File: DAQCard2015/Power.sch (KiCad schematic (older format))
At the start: 33 parts, among them CON1 BARREL_JACK, SW1 SPST, U18 APXS002A0X-SRZ, U19 APXS002A0X-SRZ, U20 APXS002A0X-SRZ, U21 CDBHD240-G, U23 LM1086

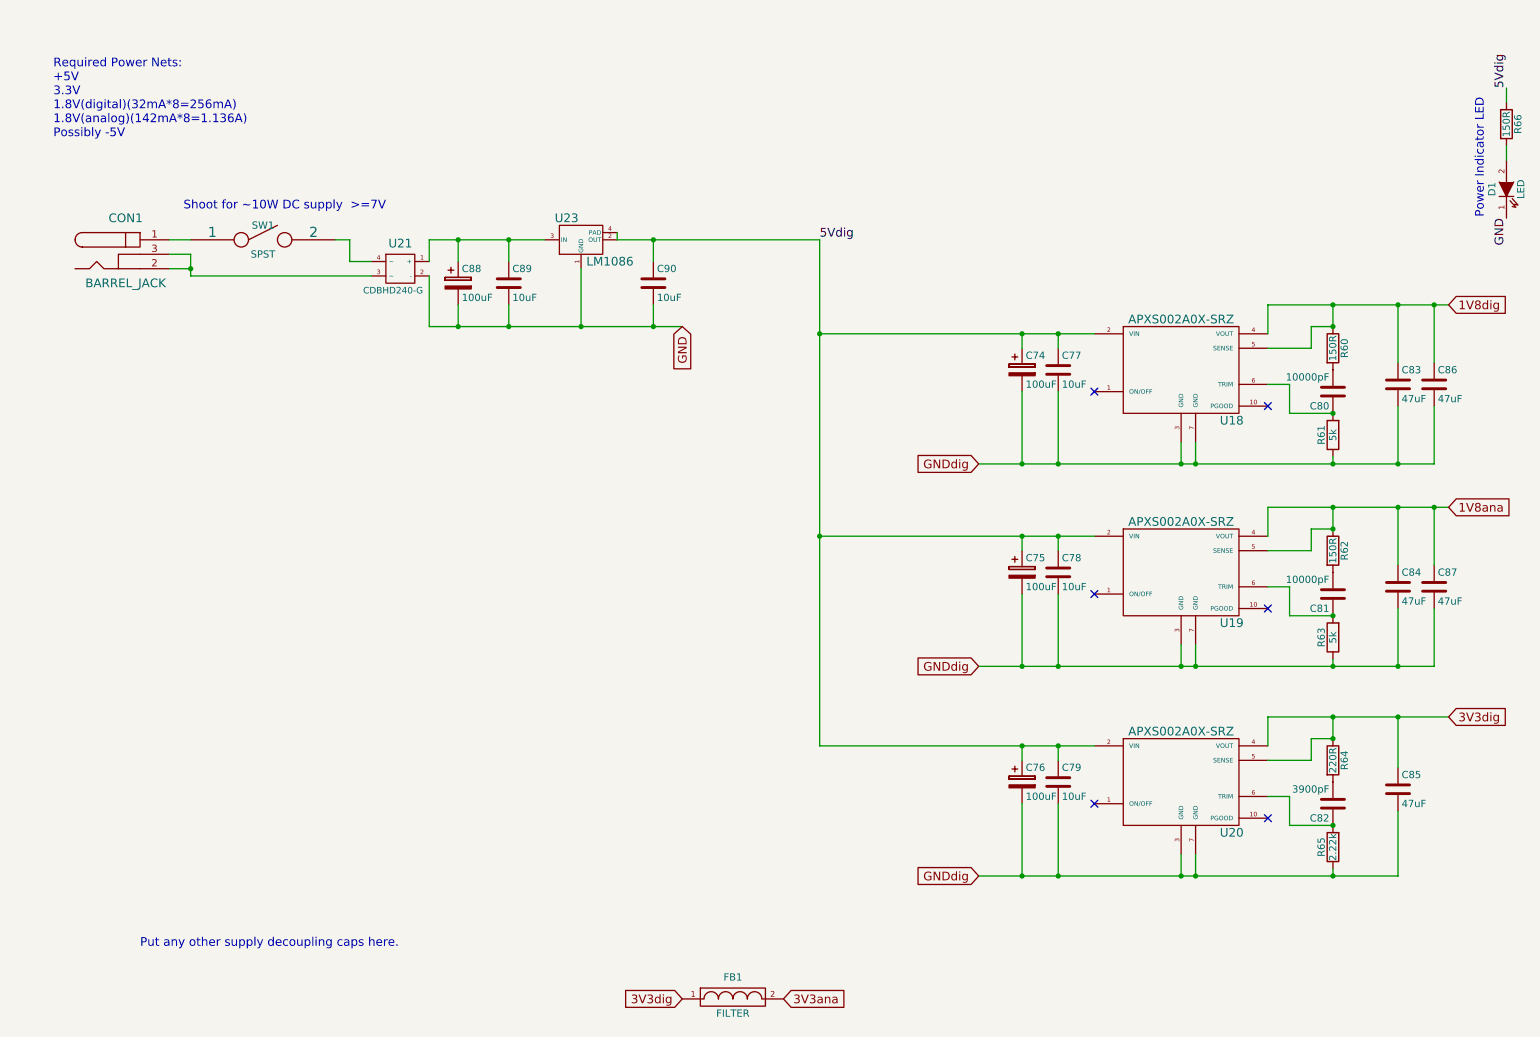
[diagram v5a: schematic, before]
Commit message: propogate previous changes to other channels and schematic
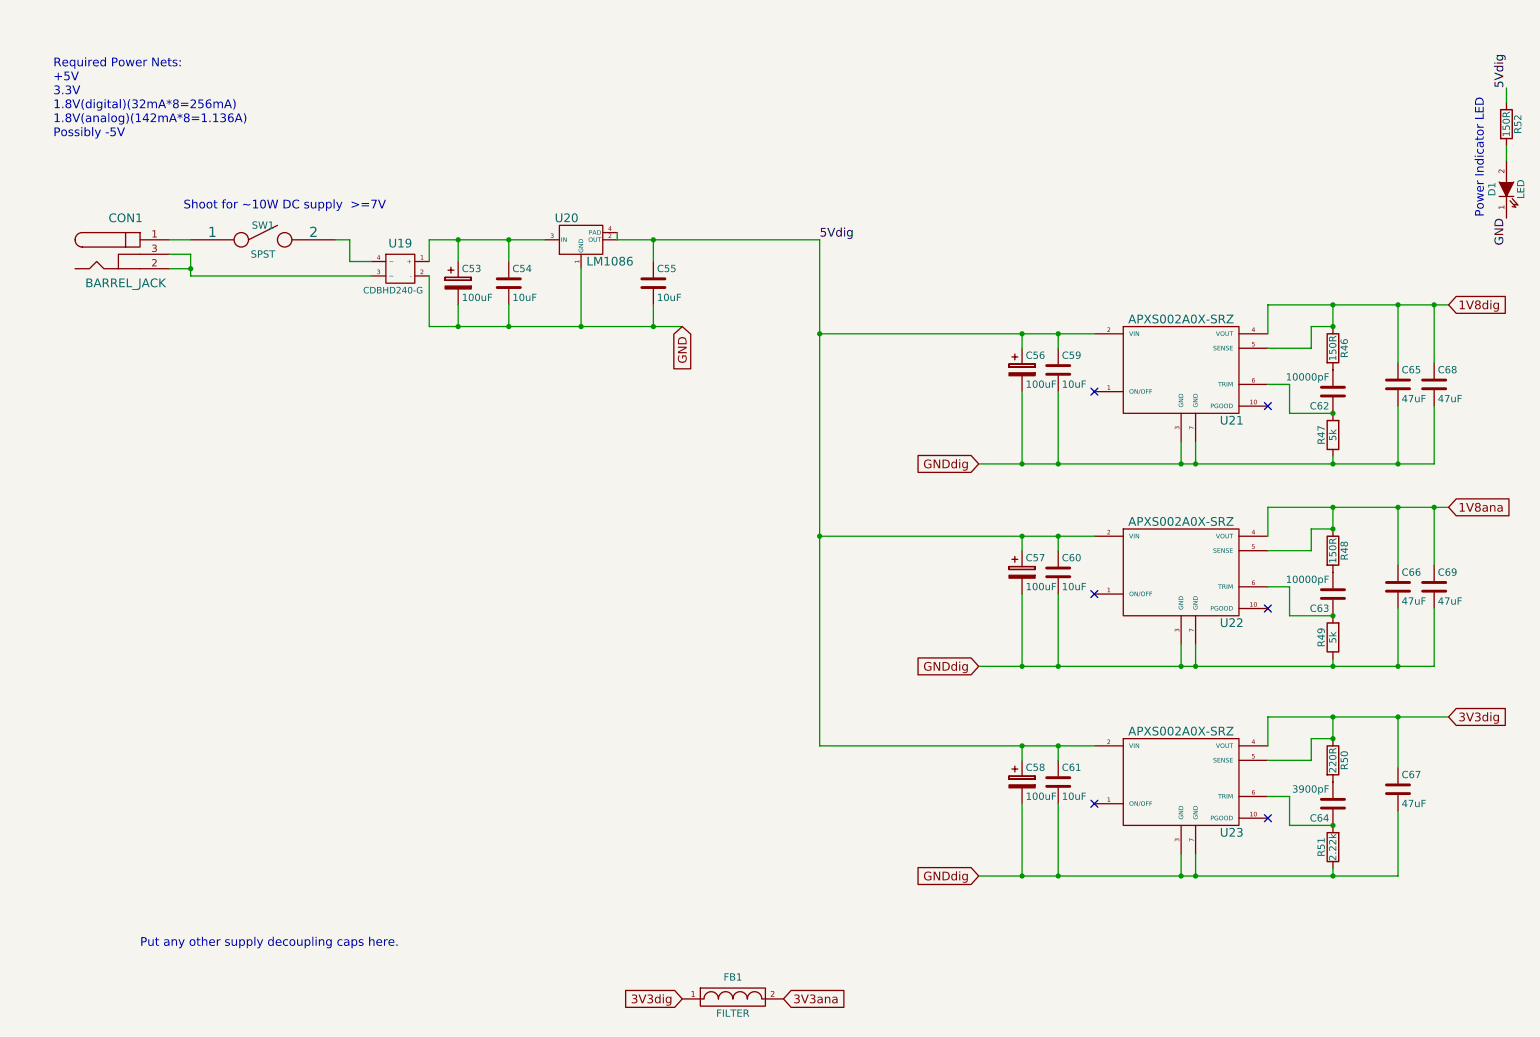
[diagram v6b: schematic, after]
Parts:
- C54: renamed from C89; footprint (none) -> Capacitors_SMD:C_0805
- C55: renamed from C90; footprint (none) -> Capacitors_SMD:C_0805
- renumbered C88 to C53, C74 to C56, C75 to C57, C76 to C58, C77 to C59, C78 to C60, C79 to C61, C80 to C62, C81 to C63, C82 to C64, C83 to C65, C84 to C66, C85 to C67, C86 to C68, C87 to C69, R60 to R46, R61 to R47, R62 to R48, R63 to R49, R64 to R50, R65 to R51, R66 to R52, U21 to U19, U23 to U20, U18 to U21, U19 to U22, U20 to U23
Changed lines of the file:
@@
 Required Power Nets:\n+5V\n3.3V\n1.8V(digital)(32mA*8=256mA)\n1.8V(analog)(142mA*8=1.136A)\nPossibly -5V
 $Comp
-L APXS002A0X-SRZ U18
+L APXS002A0X-SRZ U21
 U 1 1 55CC1B62
 P 8750 2750
-F 0 "U18" H 9100 2400 60  0000 C CNN
+F 0 "U21" H 9100 2400 60  0000 C CNN
 F 1 "APXS002A0X-SRZ" H 8750 3100 60  0000 C CNN
 F 2 "extras:APXS002A0X-SRZ" H 8400 2100 60  0001 C CNN
@@
 $EndComp
 $Comp
-L CP C74
+L CP C56
 U 1 1 55CC28F2
 P 7650 2750
-F 0 "C74" H 7675 2850 50  0000 L CNN
+F 0 "C56" H 7675 2850 50  0000 L CNN
 F 1 "100uF" H 7675 2650 50  0000 L CNN
 F 2 "extras:SMD_Cap_8mmDia" H 7688 2600 30  0001 C CNN
@@
 $EndComp
 $Comp
-L C C77
+L C C59
 U 1 1 55CC2951
 P 7900 2750
-F 0 "C77" H 7925 2850 50  0000 L CNN
+F 0 "C59" H 7925 2850 50  0000 L CNN
 F 1 "10uF" H 7925 2650 50  0000 L CNN
 F 2 "Capacitors_SMD:C_0805" H 7938 2600 30  0001 C CNN
@@
 $EndComp
 $Comp
-L R R60
+L R R46
 U 1 1 55CC29C3
 P 9800 2600
-F 0 "R60" V 9880 2600 50  0000 C CNN
+F 0 "R46" V 9880 2600 50  0000 C CNN
 F 1 "150R" V 9800 2600 50  0000 C CNN
 F 2 "Resistors_SMD:R_0603" V 9730 2600 30  0001 C CNN
@@
 $EndComp
 $Comp
-L R R61
+L R R47
 U 1 1 55CC2A10
 P 9800 3200
-F 0 "R61" V 9880 3200 50  0000 C CNN
+F 0 "R47" V 9880 3200 50  0000 C CNN
 F 1 "5k" V 9800 3200 50  0000 C CNN
 F 2 "Resistors_SMD:R_0603" V 9730 3200 30  0001 C CNN
@@
 $EndComp
 $Comp
-L C C80
+L C C62
 U 1 1 55CC2A89
 P 9800 2900
-F 0 "C80" H 9825 3000 50  0000 L CNN
+F 0 "C62" H 9825 3000 50  0000 L CNN
 F 1 "10000pF" H 9825 2800 50  0000 L CNN
 F 2 "Capacitors_SMD:C_0603" H 9838 2750 30  0001 C CNN
@@
 $EndComp
 $Comp
-L C C83
+L C C65
 U 1 1 55CC2AEA
 P 10250 2850
-F 0 "C83" H 10275 2950 50  0000 L CNN
+F 0 "C65" H 10275 2950 50  0000 L CNN
 F 1 "47uF" H 10275 2750 50  0000 L CNN
 F 2 "extras:SMD_Cap_8mmDia" H 10288 2700 30  0001 C CNN
@@
 Connection ~ 7650 3400
 $Comp
-L C C86
+L C C68
 U 1 1 55CC4361
 P 10500 2850
-F 0 "C86" H 10525 2950 50  0000 L CNN
+F 0 "C68" H 10525 2950 50  0000 L CNN
 F 1 "47uF" H 10525 2750 50  0000 L CNN
 F 2 "extras:SMD_Cap_8mmDia" H 10538 2700 30  0001 C CNN
@@
 GNDdig
 $Comp
-L APXS002A0X-SRZ U19
+L APXS002A0X-SRZ U22
 U 1 1 55CC74F0
 P 8750 4150
-F 0 "U19" H 9100 3800 60  0000 C CNN
+F 0 "U22" H 9100 3800 60  0000 C CNN
 F 1 "APXS002A0X-SRZ" H 8750 4500 60  0000 C CNN
 F 2 "extras:APXS002A0X-SRZ" H 8400 3500 60  0001 C CNN
@@
 $EndComp
 $Comp
-L CP C75
+L CP C57
 U 1 1 55CC74F7
 P 7650 4150
-F 0 "C75" H 7675 4250 50  0000 L CNN
+F 0 "C57" H 7675 4250 50  0000 L CNN
 F 1 "100uF" H 7675 4050 50  0000 L CNN
 F 2 "extras:SMD_Cap_8mmDia" H 7688 4000 30  0001 C CNN
@@
 $EndComp
 $Comp
-L C C78
+L C C60
 U 1 1 55CC74FD
 P 7900 4150
-F 0 "C78" H 7925 4250 50  0000 L CNN
+F 0 "C60" H 7925 4250 50  0000 L CNN
 F 1 "10uF" H 7925 4050 50  0000 L CNN
 F 2 "Capacitors_SMD:C_0805" H 7938 4000 30  0001 C CNN
@@
 $EndComp
 $Comp
-L R R62
+L R R48
 U 1 1 55CC7503
 P 9800 4000
-F 0 "R62" V 9880 4000 50  0000 C CNN
+F 0 "R48" V 9880 4000 50  0000 C CNN
 F 1 "150R" V 9800 4000 50  0000 C CNN
 F 2 "Resistors_SMD:R_0603" V 9730 4000 30  0001 C CNN
@@
 $EndComp
 $Comp
-L R R63
+L R R49
 U 1 1 55CC7509
 P 9800 4600
-F 0 "R63" V 9880 4600 50  0000 C CNN
+F 0 "R49" V 9880 4600 50  0000 C CNN
 F 1 "5k" V 9800 4600 50  0000 C CNN
 F 2 "Resistors_SMD:R_0603" V 9730 4600 30  0001 C CNN
@@
 $EndComp
 $Comp
-L C C81
+L C C63
 U 1 1 55CC750F
 P 9800 4300
-F 0 "C81" H 9825 4400 50  0000 L CNN
+F 0 "C63" H 9825 4400 50  0000 L CNN
 F 1 "10000pF" H 9825 4200 50  0000 L CNN
 F 2 "Capacitors_SMD:C_0603" H 9838 4150 30  0001 C CNN
@@
 $EndComp
 $Comp
-L C C84
+L C C66
 U 1 1 55CC7515
 P 10250 4250
-F 0 "C84" H 10275 4350 50  0000 L CNN
+F 0 "C66" H 10275 4350 50  0000 L CNN
 F 1 "47uF" H 10275 4150 50  0000 L CNN
 F 2 "extras:SMD_Cap_8mmDia" H 10288 4100 30  0001 C CNN
@@
 Connection ~ 7650 4800
 $Comp
-L C C87
+L C C69
 U 1 1 55CC7546
 P 10500 4250
-F 0 "C87" H 10525 4350 50  0000 L CNN
+F 0 "C69" H 10525 4350 50  0000 L CNN
 F 1 "47uF" H 10525 4150 50  0000 L CNN
 F 2 "extras:SMD_Cap_8mmDia" H 10538 4100 30  0001 C CNN
@@
 GNDdig
 $Comp
-L APXS002A0X-SRZ U20
+L APXS002A0X-SRZ U23
 U 1 1 55CC7C26
 P 8750 5600
-F 0 "U20" H 9100 5250 60  0000 C CNN
+F 0 "U23" H 9100 5250 60  0000 C CNN
 F 1 "APXS002A0X-SRZ" H 8750 5950 60  0000 C CNN
 F 2 "extras:APXS002A0X-SRZ" H 8400 4950 60  0001 C CNN
@@
 $EndComp
 $Comp
-L CP C76
+L CP C58
 U 1 1 55CC7C2D
 P 7650 5600
-F 0 "C76" H 7675 5700 50  0000 L CNN
+F 0 "C58" H 7675 5700 50  0000 L CNN
 F 1 "100uF" H 7675 5500 50  0000 L CNN
 F 2 "extras:SMD_Cap_8mmDia" H 7688 5450 30  0001 C CNN
@@
 $EndComp
 $Comp
-L C C79
+L C C61
 U 1 1 55CC7C33
 P 7900 5600
-F 0 "C79" H 7925 5700 50  0000 L CNN
+F 0 "C61" H 7925 5700 50  0000 L CNN
 F 1 "10uF" H 7925 5500 50  0000 L CNN
 F 2 "Capacitors_SMD:C_0805" H 7938 5450 30  0001 C CNN
@@
 $EndComp
 $Comp
-L R R64
+L R R50
 U 1 1 55CC7C39
 P 9800 5450
-F 0 "R64" V 9880 5450 50  0000 C CNN
+F 0 "R50" V 9880 5450 50  0000 C CNN
 F 1 "220R" V 9800 5450 50  0000 C CNN
 F 2 "Resistors_SMD:R_0603" V 9730 5450 30  0001 C CNN
@@
 $EndComp
 $Comp
-L R R65
+L R R51
 U 1 1 55CC7C3F
 P 9800 6050
-F 0 "R65" V 9880 6050 50  0000 C CNN
+F 0 "R51" V 9880 6050 50  0000 C CNN
 F 1 "2.22k" V 9800 6050 50  0000 C CNN
 F 2 "Resistors_SMD:R_0603" V 9730 6050 30  0001 C CNN
@@
 $EndComp
 $Comp
-L C C82
+L C C64
 U 1 1 55CC7C45
 P 9800 5750
-F 0 "C82" H 9825 5850 50  0000 L CNN
+F 0 "C64" H 9825 5850 50  0000 L CNN
 F 1 "3900pF" H 9825 5650 50  0000 L CNN
 F 2 "Capacitors_SMD:C_0603" H 9838 5600 30  0001 C CNN
@@
 $EndComp
 $Comp
-L C C85
+L C C67
 U 1 1 55CC7C4B
 P 10250 5650
-F 0 "C85" H 10275 5750 50  0000 L CNN
+F 0 "C67" H 10275 5750 50  0000 L CNN
 F 1 "47uF" H 10275 5550 50  0000 L CNN
 F 2 "extras:SMD_Cap_8mmDia" H 10288 5500 30  0001 C CNN
@@
 Shoot for ~~10W DC supply  >=7V
 $Comp
-L CP C88
+L CP C53
 U 1 1 55CD0228
 P 3750 2150
-F 0 "C88" H 3775 2250 50  0000 L CNN
+F 0 "C53" H 3775 2250 50  0000 L CNN
 F 1 "100uF" H 3775 2050 50  0000 L CNN
 F 2 "extras:SMD_Cap_8mmDia" H 3788 2000 30  0001 C CNN
@@
 $EndComp
 $Comp
-L LM1086 U23
+L LM1086 U20
 U 1 1 55EA84EC
 P 4600 2050
-F 0 "U23" H 4500 2400 60  0000 C CNN
+F 0 "U20" H 4500 2400 60  0000 C CNN
 F 1 "LM1086" H 4800 2100 60  0000 C CNN
 F 2 "extras:TO-263-4" H 4600 2050 60  0001 C CNN
@@
 Connection ~ 4100 1850
 $Comp
-L R R66
+L R R52
 U 1 1 55EAAA38
 P 11000 1050
-F 0 "R66" V 11080 1050 50  0000 C CNN
+F 0 "R52" V 11080 1050 50  0000 C CNN
 F 1 "150R" V 11000 1050 50  0000 C CNN
 F 2 "Resistors_SMD:R_0603" V 10930 1050 30  0001 C CNN
@@
 Connection ~ 5100 2450
 $Comp
-L CDBHD240-G U21
+L CDBHD240-G U19
 U 1 1 55EAC9BE
 P 3350 2050
-F 0 "U21" H 3350 2225 60  0000 C CNN
+F 0 "U19" H 3350 2225 60  0000 C CNN
 F 1 "CDBHD240-G" H 3400 1900 45  0000 C CNN
 F 2 "extras:mini-DIP4" H 3350 2050 60  0001 C CNN
@@
 	4850 1850 4850 1800
 $Comp
-L C C89
+L C C54
 U 1 1 55EB2165
 P 4100 2150
-F 0 "C89" H 4125 2250 50  0000 L CNN
+F 0 "C54" H 4125 2250 50  0000 L CNN
 F 1 "10uF" H 4125 2050 50  0000 L CNN
-F 2 "" H 4138 2000 30  0000 C CNN
+F 2 "Capacitors_SMD:C_0805" H 4138 2000 30  0001 C CNN
 F 3 "" H 4100 2150 60  0000 C CNN
 	1    4100 2150
@@
 $EndComp
 $Comp
-L C C90
+L C C55
 U 1 1 55EB21EC
 P 5100 2150
-F 0 "C90" H 5125 2250 50  0000 L CNN
+F 0 "C55" H 5125 2250 50  0000 L CNN
 F 1 "10uF" H 5125 2050 50  0000 L CNN
-F 2 "" H 5138 2000 30  0000 C CNN
+F 2 "Capacitors_SMD:C_0805" H 5138 2000 30  0001 C CNN
 F 3 "" H 5100 2150 60  0000 C CNN
 	1    5100 2150

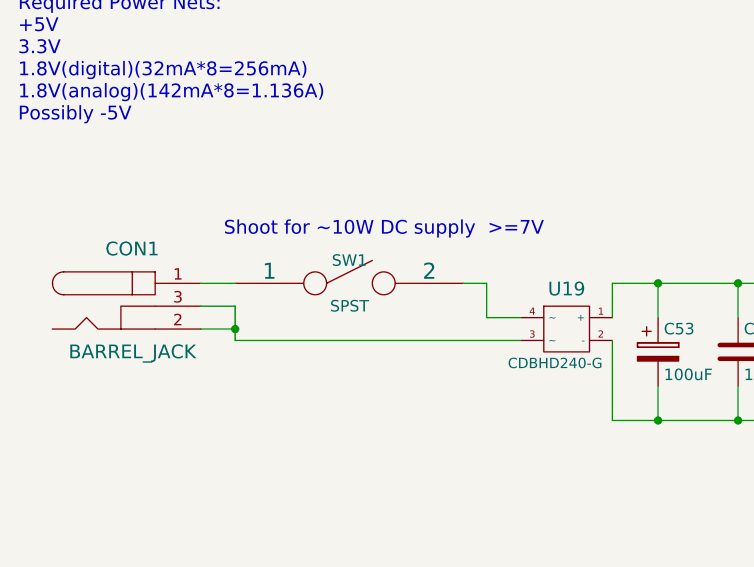
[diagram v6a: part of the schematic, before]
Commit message: Reroutes LVDS signals to give pairs proper impedances
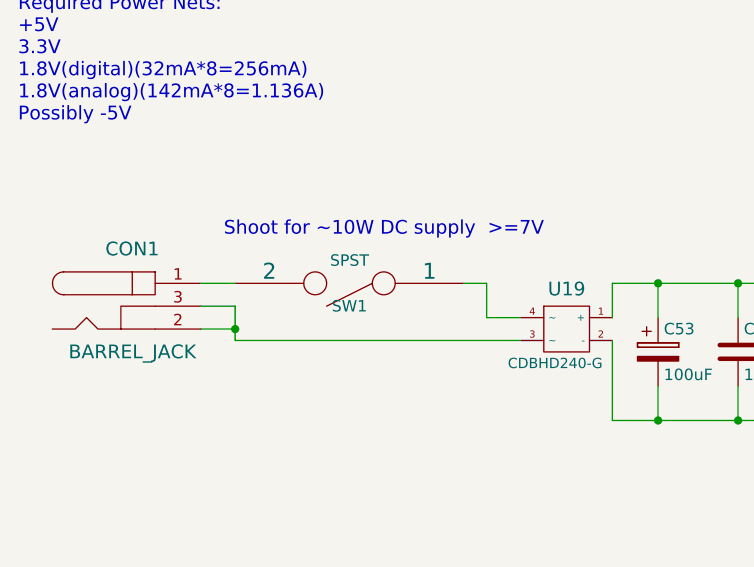
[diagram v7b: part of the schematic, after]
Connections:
- net at CON1.1: now also SW1.2; no longer SW1.1
- net at U19.4 (~~): now also SW1.1; no longer SW1.2
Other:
- moved on the sheet: SW1
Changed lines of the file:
@@
 F 3 "" H 2400 1850 60  0000 C CNN
 	1    2400 1850
-	1    0    0    -1
+	-1   0    0    1
 $EndComp
 Wire Wire Line
